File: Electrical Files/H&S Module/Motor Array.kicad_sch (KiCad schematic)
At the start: 24 parts, among them M13 PPN7PA12C1, M14 PPN7PA12C1, M15 PPN7PA12C1, M16 PPN7PA12C1, M17 PPN7PA12C1, M18 PPN7PA12C1, M19 PPN7PA12C1, M20 PPN7PA12C1, M21 PPN7PA12C1, M22 PPN7PA12C1, M23 PPN7PA12C1, M24 PPN7PA12C1, Q1 BSR802NL6327HTSA1, Q2 BSR802NL6327HTSA1, Q3 BSR802NL6327HTSA1, Q8 BSR802NL6327HTSA1

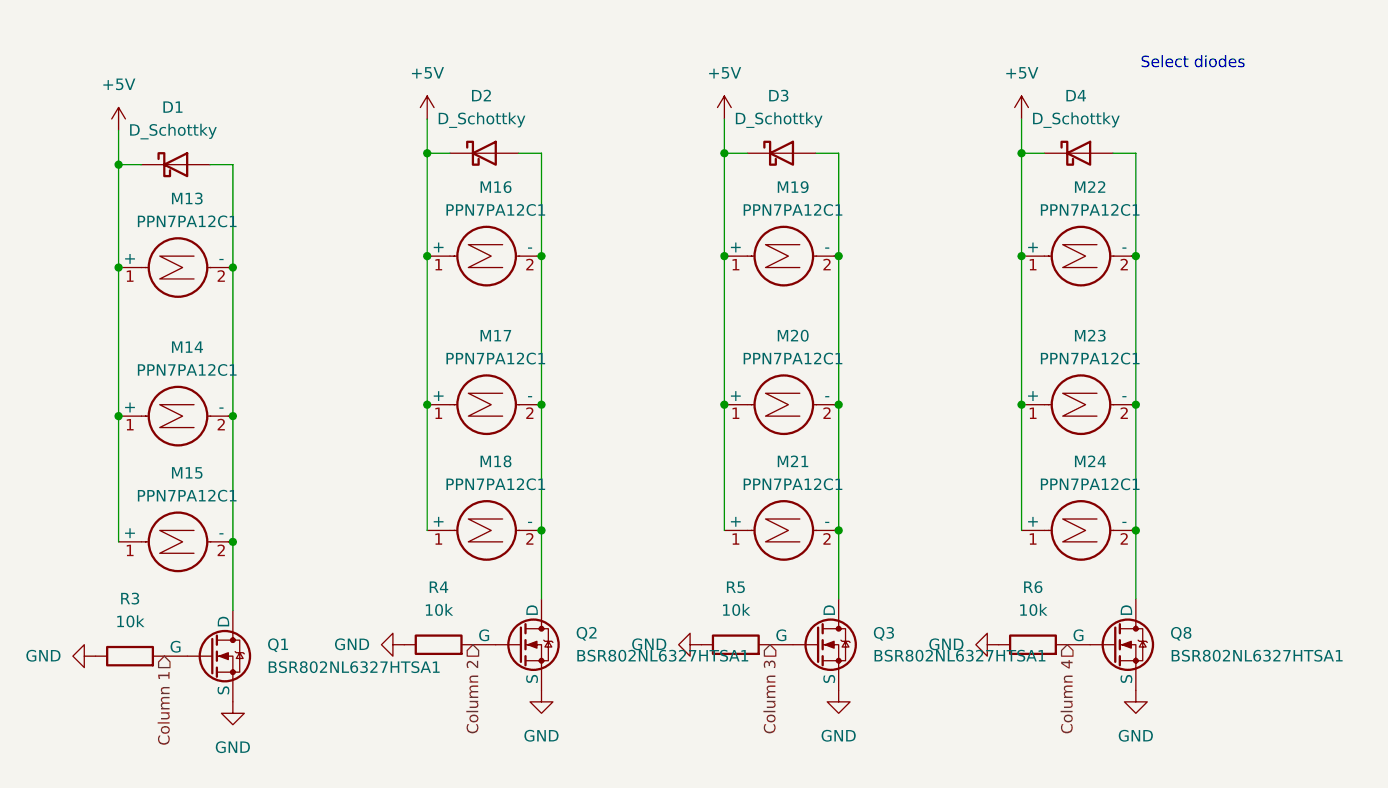
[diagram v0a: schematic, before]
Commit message: New motor
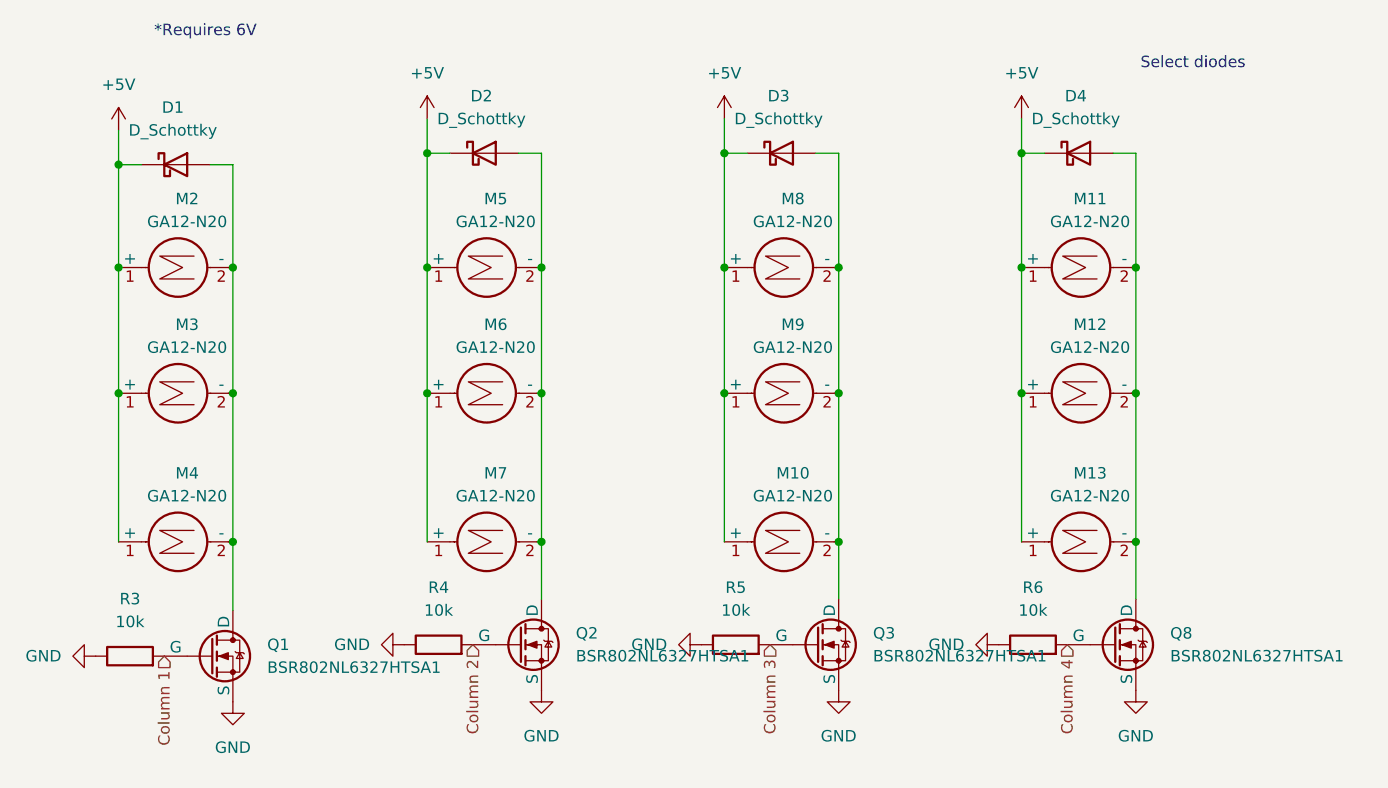
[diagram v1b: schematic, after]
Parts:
- removed M14, M15, M16, M17, M18, M19, M20, M21, M22, M23, M24: PPN7PA12C1, Gnome Foot Library:01x02 Jumper Pads, symbol Motor:Motor_DC
- added M10, M11, M12, M2, M3, M4, M5, M6, M7, M8, M9: GA12-N20, Pozzo Lab:GA12-N20, symbol Motor:Motor_DC
- M13: value PPN7PA12C1 -> GA12-N20; footprint Gnome Foot Library:01x02 Jumper Pads -> Pozzo Lab:GA12-N20
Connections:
- net +5V: now also M10.1 (+), M11.1 (+), M12.1 (+), M2.1 (+), M3.1 (+), M4.1 (+), M5.1 (+), M6.1 (+), M7.1 (+), M8.1 (+), M9.1 (+)
- net at D3.2 (A), Q3.1 (D): now also M10.2 (-), M8.2 (-), M9.2 (-)
- net at D2.2 (A), Q2.1 (D): now also M5.2 (-), M6.2 (-), M7.2 (-)
- net at D1.2 (A), Q1.1 (D): now also M2.2 (-), M3.2 (-), M4.2 (-); no longer M13.2 (-)
- net at D4.2 (A), Q8.1 (D): now also M13.2 (-), M11.2 (-), M12.2 (-)
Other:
- note added: "*Requires 6V"
